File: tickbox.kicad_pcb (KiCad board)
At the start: 2 copper layers, 1 part, among them IC1 R5F10RLAGFB#10

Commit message: Sketch PCB layout
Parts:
- added BT1: Battery_Cell, 3rdparty:COIN_HOLDER_TH, F.Cu at (170.3, 109.9)
- added BZ1: Buzzer, Buzzer_Beeper:Buzzer_TDK_PS1240P02BT_D12.2mm_H6.5mm, F.Cu at (132.4, 94.2)
- added C1: 8pf, Capacitor_SMD:C_1206_3216Metric_Pad1.33x1.80mm_HandSolder, F.Cu at (157.9, 109.0)
- added C2: 8pf, Capacitor_SMD:C_1206_3216Metric_Pad1.33x1.80mm_HandSolder, F.Cu at (159.9, 107.0)
- added C4: 0.47uF, Capacitor_SMD:C_1206_3216Metric_Pad1.33x1.80mm_HandSolder, F.Cu at (161.8, 97.2)
- added C5: 0.1uF, Capacitor_SMD:C_1206_3216Metric_Pad1.33x1.80mm_HandSolder, F.Cu at (161.0, 92.0)
- added D1: ~, 3rdparty:VI-402, B.Cu at (144.0, 87.5)
- added D2: LED, LED_SMD:LED_1206_3216Metric_Pad1.42x1.75mm_HandSolder, B.Cu at (173.9, 101.6)
- added J1: Conn_01x03_Pin, Connector_PinHeader_2.54mm:PinHeader_1x03_P2.54mm_Vertical, F.Cu at (138.6, 112.1)
- added J2: Conn_01x02_Pin, Connector_PinHeader_2.54mm:PinHeader_1x02_P2.54mm_Vertical, F.Cu at (174.3, 112.8)
- added Q1: BC848, Package_TO_SOT_SMD:SOT-23, F.Cu at (129.8, 105.5)
- added R1: 10k, Resistor_SMD:R_1206_3216Metric_Pad1.30x1.75mm_HandSolder, F.Cu at (134.3, 115.4)
- added R10: 10k, Resistor_SMD:R_1206_3216Metric_Pad1.30x1.75mm_HandSolder, F.Cu at (165.4, 100.8)
- added R11: 10k, Resistor_SMD:R_1206_3216Metric_Pad1.30x1.75mm_HandSolder, F.Cu at (163.6, 99.0)
- added R12: 10k, Resistor_SMD:R_1206_3216Metric_Pad1.30x1.75mm_HandSolder, F.Cu at (139.5, 115.4)
- added R13: 1k, Resistor_SMD:R_1206_3216Metric_Pad1.30x1.75mm_HandSolder, F.Cu at (130.0, 110.3)
- added R2: 10k, Resistor_SMD:R_1206_3216Metric_Pad1.30x1.75mm_HandSolder, F.Cu at (161.8, 105.2)
- added R3: 1k, Resistor_SMD:R_1206_3216Metric_Pad1.30x1.75mm_HandSolder, F.Cu at (152.5, 114.6)
- added R4: 2k, Resistor_SMD:R_1206_3216Metric_Pad1.30x1.75mm_HandSolder, F.Cu at (150.1, 110.5)
- added R5: 10k, Resistor_SMD:R_1206_3216Metric_Pad1.30x1.75mm_HandSolder, F.Cu at (120.7, 88.9)
- added R6: 10k, Resistor_SMD:R_1206_3216Metric_Pad1.30x1.75mm_HandSolder, F.Cu at (125.1, 107.7)
- added R7: 4.7k, Resistor_SMD:R_1206_3216Metric_Pad1.30x1.75mm_HandSolder, F.Cu at (133.8, 108.5)
- added R9: 1.6k, Resistor_SMD:R_1206_3216Metric_Pad1.30x1.75mm_HandSolder, B.Cu at (173.9, 106.9)
- added SW1: SW_MEC_5G, Button_Switch_THT:SW_SPST_Omron_B3F-315x_Angled, F.Cu at (173.2, 89.9)
- added SW2: SW_MEC_5G, Button_Switch_THT:SW_SPST_Omron_B3F-315x_Angled, F.Cu at (119.2, 97.5)
- added SW3: SW_MEC_5G, Button_Switch_THT:SW_SPST_Omron_B3F-315x_Angled, F.Cu at (119.2, 109.6)
- added Y1: 32.768 kHz, Crystal:Crystal_DS26_D2.0mm_L6.0mm_Vertical, F.Cu at (156.4, 104.2)
- moved IC1 6.75 mm to (149.2, 97.8)
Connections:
- IC1 pad 10: unconnected-(IC1-P122/X2/EXCLK-Pad10) -> Net-(IC1-P122/X2/EXCLK)
- IC1 pad 11: unconnected-(IC1-P121/X1-Pad11) -> Net-(IC1-P121/X1)
- IC1 pad 19: unconnected-(IC1-P127/CAPH-Pad19) -> /SWIN
- IC1 pad 20: unconnected-(IC1-P126/CAPL-Pad20) -> /SWOUT
- IC1 pad 37: unconnected-(IC1-P50/INTP5/SEG7/(PCLBUZ0)-Pad37) -> Net-(IC1-P50/INTP5/SEG7/(PCLBUZ0))
- IC1 pad 39: unconnected-(IC1-P16/SI01/INTP2/SEG5-Pad39) -> Net-(IC1-P16/SI01/INTP2/SEG5)
- IC1 pad 51: unconnected-(IC1-P130-Pad51) -> Net-(D2-K)
- IC1 pad 63: unconnected-(IC1-P140/TO00/PCLBUZ0/SEG27/(INTP6)-Pad63) -> /PCLBUZ0
- IC1 pad 9: unconnected-(IC1-P137/INTP0-Pad9) -> Net-(IC1-P137/INTP0)
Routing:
- net /COM: track 0.00 -> 103.3 mm, vias 0 -> 1
- net VDD: track 0.00 -> 80.3 mm, vias 0 -> 1
- net Net-(D2-K): track 0.00 -> 36.4 mm, vias 0 -> 1
- net Net-(IC1-P16/SI01/INTP2/SEG5): track 0.00 -> 34.7 mm
- net Net-(IC1-P50/INTP5/SEG7/(PCLBUZ0)): track 0.00 -> 32.7 mm
- net /SEG37: track 0.00 -> 30.1 mm, vias 0 -> 1
- net /SEG3: track 0.00 -> 27.9 mm, vias 0 -> 2
- net /SEG36: track 0.00 -> 27.8 mm, vias 0 -> 1
- net /SEG0: track 0.00 -> 26.9 mm, vias 0 -> 1
- net /SEG2: track 0.00 -> 26.6 mm, vias 0 -> 2
- net /SEG6: track 0.00 -> 26.0 mm, vias 0 -> 2
- net /SEG35: track 0.00 -> 25.9 mm, vias 0 -> 1
- net GND: track 0.00 -> 25.5 mm, vias 0 -> 3
- net Net-(IC1-P137/INTP0): track 0.00 -> 25.3 mm
- net /SEG1: track 0.00 -> 24.3 mm, vias 0 -> 1
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- added copper zone on B.Cu, net GND
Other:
- board outline added: 60.6 x 36.6 mm
- copper layers 2 -> 4

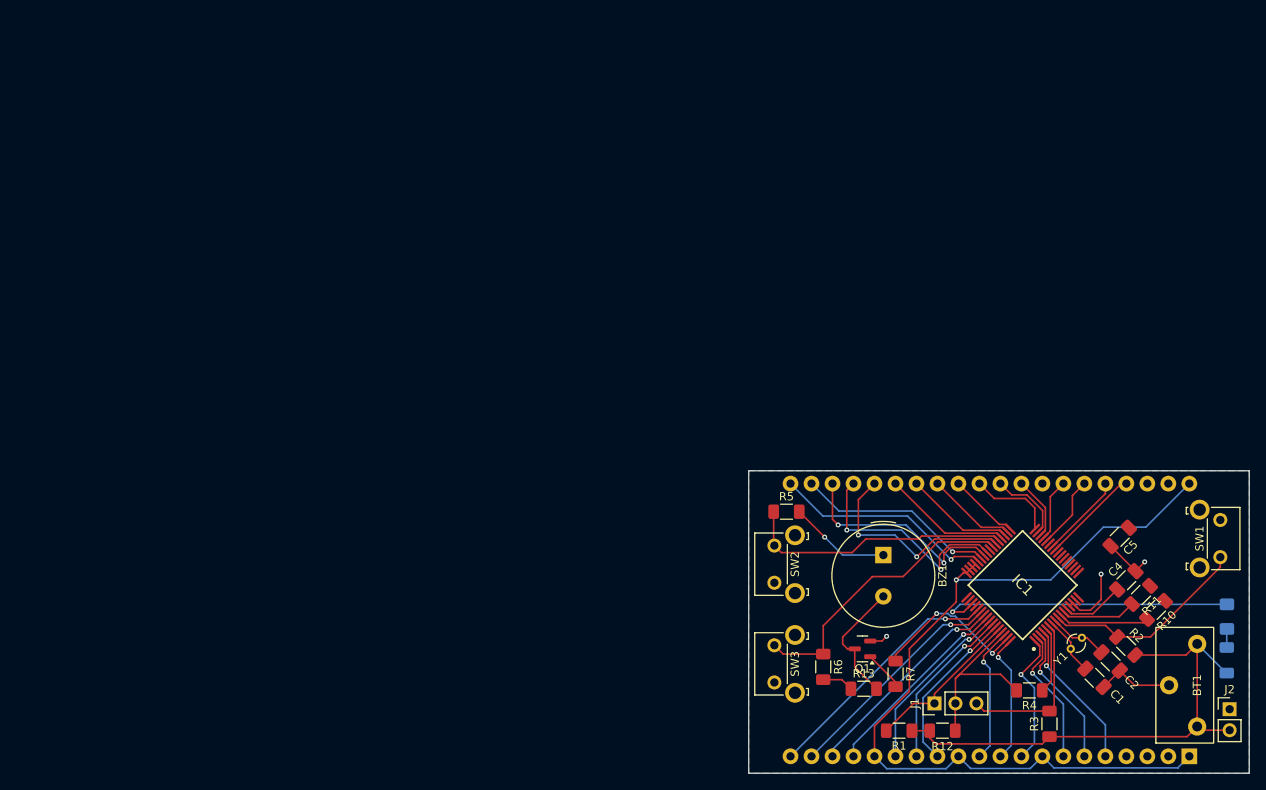
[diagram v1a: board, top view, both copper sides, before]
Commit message: add coin holder etc
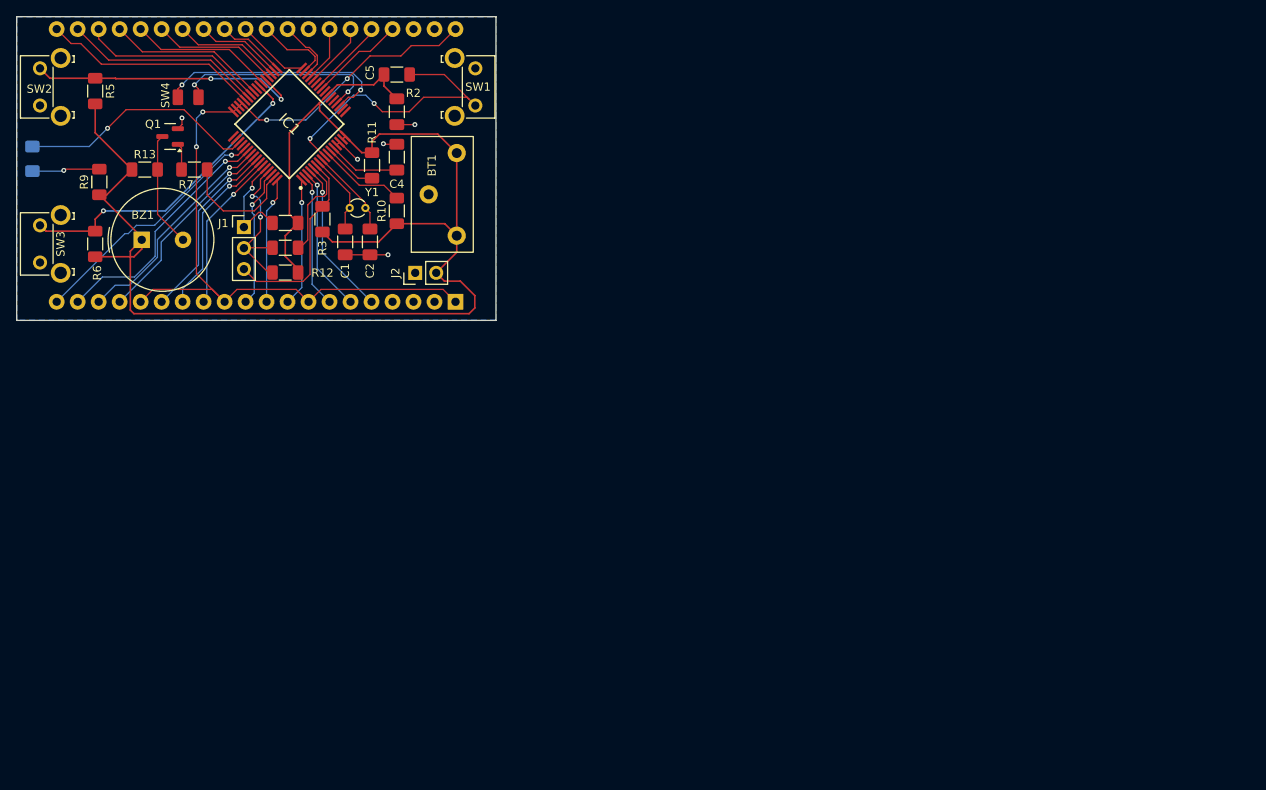
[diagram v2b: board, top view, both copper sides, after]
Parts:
- added SW4: SW_MEC_5G, 3rdparty:Wire_pads, F.Cu at (49.5, 37.2)
- R9: moved to F.Cu
- moved D2 154.8 mm to (29.4, 46.2)
- moved R9 148.2 mm to (37.5, 49.0)
- moved R2 112.1 mm to (73.5, 36.0), turned to 180 degrees
- moved J2 111.8 mm to (75.7, 60.0), turned to 90 degrees
- moved BT1 107.5 mm to (80.8, 50.5)
- moved R13 107.3 mm to (43.0, 47.5)
- moved R3 107.1 mm to (64.5, 53.5)
- moved R11 106.6 mm to (70.5, 47.0), turned to -90 degrees
- moved SW2 106.0 mm to (30.3, 39.8)
- moved SW1 105.4 mm to (83.0, 35.2)
- moved C1 104.9 mm to (67.2, 56.2), turned to 90 degrees
- moved IC1 104.8 mm to (60.5, 42.0)
- moved R4 104.8 mm to (60.0, 57.0)
- moved R7 104.5 mm to (49.0, 47.5), turned to 180 degrees
- moved D1 104.5 mm to (55.2, 32.5)
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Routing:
- net VDD: track 80.3 -> 181.4 mm, vias 1 -> 0
- net /SWIN: track 0.00 -> 28.9 mm, vias 0 -> 2
- net /SWOUT: track 0.00 -> 25.6 mm, vias 0 -> 2
- net GND: track 25.5 -> 14.3 mm, vias 3 -> 5
- net Net-(IC1-P137/INTP0): track 25.3 -> 35.5 mm, vias 0 -> 2
- net /SEG6: track 26.0 -> 17.4 mm, vias 2 -> 0
- net /SEG3: track 27.9 -> 19.4 mm, vias 2 -> 0
- net Net-(D2-K): track 36.4 -> 29.2 mm
- net /TOOLTXD: track 19.4 -> 12.9 mm, vias 0 -> 1
- net Net-(D2-A): track 2.25 -> 8.20 mm, vias 0 -> 1
- net /PCLBUZ0: track 19.1 -> 14.6 mm, vias 2 -> 0
- net /TOOL0: track 8.06 -> 12.4 mm
- net /SEG2: track 26.6 -> 22.4 mm, vias 2 -> 0
- net /RESET: track 19.9 -> 23.7 mm
- net Net-(IC1-P16/SI01/INTP2/SEG5): track 34.7 -> 38.5 mm, vias 0 -> 2
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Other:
- board size 60.6 x 36.6 mm -> 58 x 36.8 mm
- rule pad_to_mask_clearance: 0 -> 0.038
